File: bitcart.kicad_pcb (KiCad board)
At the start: 4 copper layers, 136.6 x 54.6 mm, 78 parts, among them J1 Conn_01x03, J11 USB_OTG, J17 Molex 470531000, J2 Conn_02x07_Odd_Even, J3 Conn_01x03, Q1 SI7430DP, Q2 MMBTA06LT1G, U1 MP8008, U10 MagJack-A70-112-331N126, U11 EMC2301-1-ACZL-TR, U12 MDT320M01001, U2 FOD817S, U3 750310744, U4 TPD4EUSB30, U5 74LVC1G07SE-7, U6 TL432DBZ, U7 TPD4EUSB30, U8 TPD4EUSB30, U9 74LVC1G07SE-7

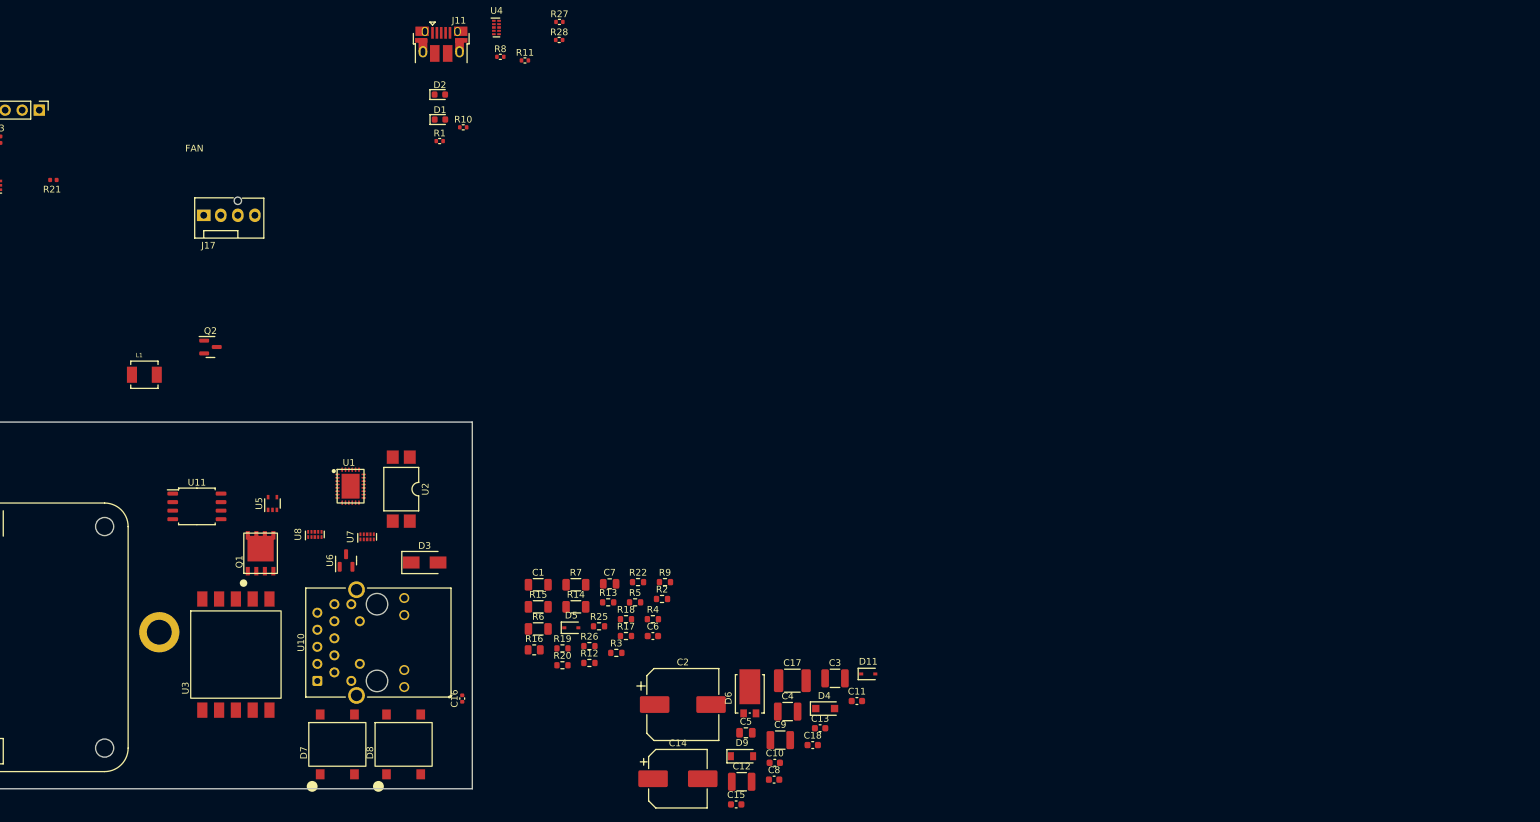
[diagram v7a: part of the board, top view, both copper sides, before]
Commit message: changed PoE transformer to Wurth 7491194912
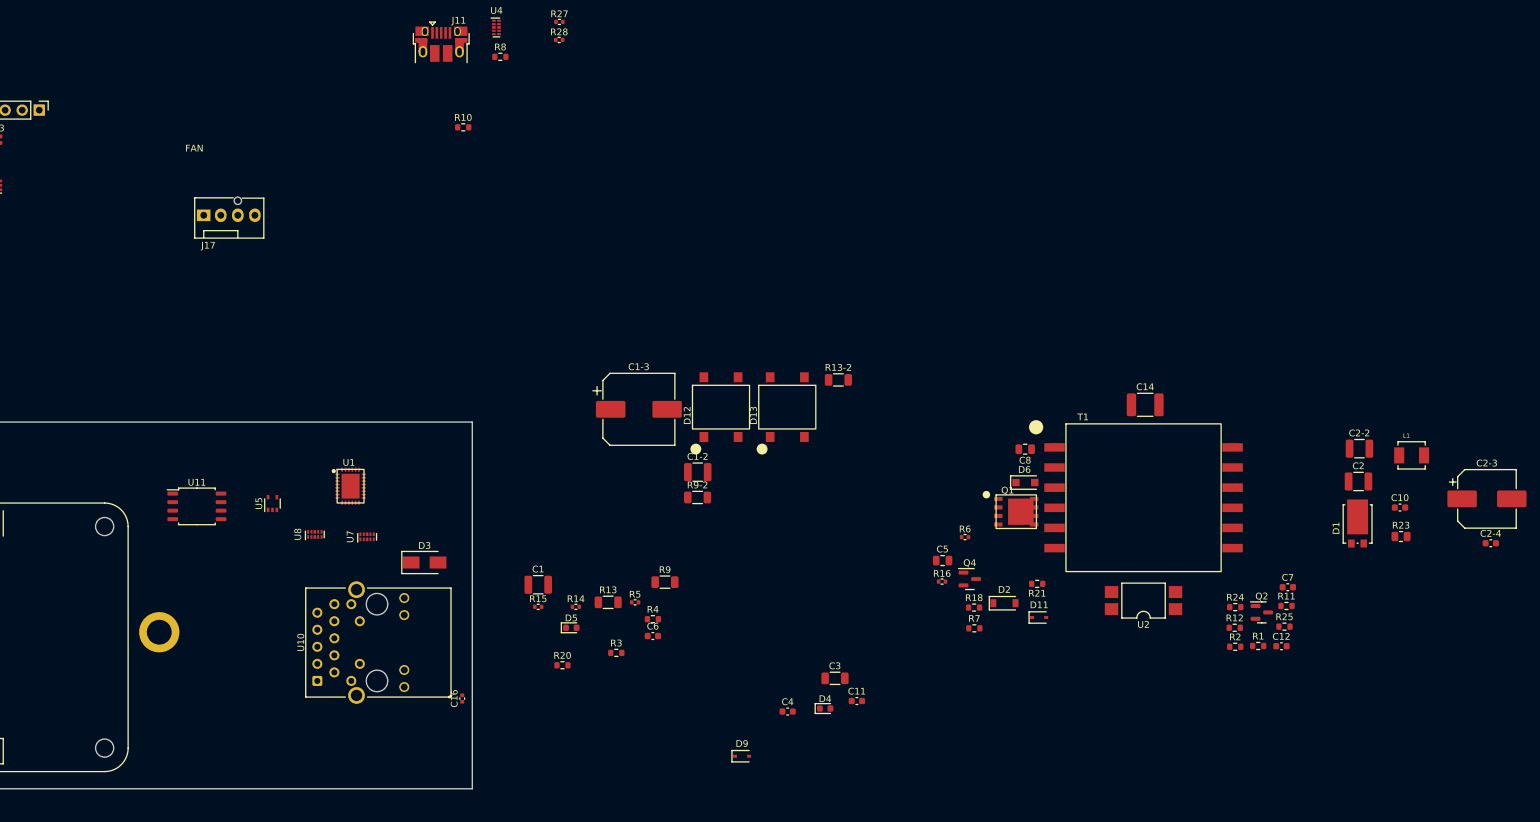
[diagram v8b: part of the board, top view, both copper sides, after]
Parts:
- removed C13: 680pF, Capacitor_SMD:C_0603_1608Metric
- removed C15: 0.1uF, Capacitor_SMD:C_0603_1608Metric
- removed C17: 1nF, 2000V, Capacitor_SMD:C_1812_4532Metric
- removed C18: 1uF, Capacitor_SMD:C_0603_1608Metric
- removed C9: 22uF, Capacitor_SMD:C_1210_3225Metric
- removed D7, D8: DF01S, bitcart:DF01S
- removed R17: 2k, Resistor_SMD:R_0603_1608Metric
- removed R19: 49.9k, Resistor_SMD:R_0603_1608Metric
- removed R22: 1k, Resistor_SMD:R_0603_1608Metric
- removed R26: 191k, Resistor_SMD:R_0603_1608Metric
- removed U3: 750310744, bitcart:750310744
- removed U6: TL432DBZ, Package_TO_SOT_SMD:SOT-23
- added C1-2: 2.2uF, Capacitor_SMD:C_1210_3225Metric, F.Cu at (216.1, 205.1)
- added C1-3: 47uF, Capacitor_SMD:CP_Elec_10x10.5, F.Cu at (207.4, 195.7)
- added C2-2: 22uF, Capacitor_SMD:C_1210_3225Metric, F.Cu at (314.7, 201.6)
- added C2-3: 220uF, Capacitor_SMD:CP_Elec_8x10.5, F.Cu at (333.7, 209.1)
- added C2-4: 0.1uF, Capacitor_SMD:C_0603_1608Metric, F.Cu at (334.2, 215.7)
- added D12: DF01S, bitcart:DF01S, F.Cu at (219.6, 195.4)
- added D13: DF01S, bitcart:DF01S, F.Cu at (229.5, 195.4)
- added Q4: MMBTA06LT1G, Package_TO_SOT_SMD:SOT-23, F.Cu at (256.6, 221.0)
- added R13-2: 20k, Resistor_SMD:R_1206_3216Metric, F.Cu at (237.1, 191.3)
- added R23: 20, Resistor_SMD:R_0805_2012Metric, F.Cu at (320.9, 214.7)
- added R24: 2k, Resistor_SMD:R_0603_1608Metric, F.Cu at (296.2, 225.2)
- added R9-2: 0.082, Resistor_SMD:R_1206_3216Metric, F.Cu at (216.1, 208.9)
- added T1: 7491194912, bitcart:7491194912, F.Cu at (282.5, 208.9)
- C1: value 0.1uF, 100V -> 2.2uF; footprint Resistor_SMD:R_1206_3216Metric -> Capacitor_SMD:C_1210_3225Metric
- C10: value 0.1uF -> 0.47nF
- C12: value 22uF -> 680pF; footprint Capacitor_SMD:C_1210_3225Metric -> Capacitor_SMD:C_0603_1608Metric
- C14: value 220uF -> 1nF, 2000V; footprint Capacitor_SMD:CP_Elec_8x10.5 -> Capacitor_SMD:C_1812_4532Metric
- C2: value 47uF -> 22uF; footprint Capacitor_SMD:CP_Elec_10x10.5 -> Capacitor_SMD:C_1210_3225Metric
- C3: value 2.2uF -> 0.1uF, 100V; footprint Capacitor_SMD:C_1210_3225Metric -> Resistor_SMD:R_1206_3216Metric
- C4: value 2.2uF -> 1uF; footprint Capacitor_SMD:C_1210_3225Metric -> Capacitor_SMD:C_0603_1608Metric
- C5: value 0.1uF -> 4.7uF
- C7: value 4.7uF -> 0.1uF; footprint Capacitor_SMD:C_0805_2012Metric -> Capacitor_SMD:C_0603_1608Metric
- C8: value 0.47nF -> 0.1uF; footprint Capacitor_SMD:C_0603_1608Metric -> Capacitor_SMD:C_0805_2012Metric
- D1: value LED Red -> SBR8U60P5-13; footprint LED_SMD:LED_0603_1608Metric -> bitcart:SBR8U60P5-13
- D2: value LED Green -> 9.1V; footprint LED_SMD:LED_0603_1608Metric -> Diode_SMD:D_SOD-123
- D4: value BAV21 -> LED Green; footprint Diode_SMD:D_SOD-123F -> LED_SMD:LED_0603_1608Metric
- D5: value 1N4148WS -> LED Red; footprint Diode_SMD:D_SOD-323 -> LED_SMD:LED_0603_1608Metric
- D6: value SBR8U60P5-13 -> BAV21; footprint bitcart:SBR8U60P5-13 -> Diode_SMD:D_SOD-123F
- D9: value 9.1V -> 1N4148WS; footprint Diode_SMD:D_SOD-123 -> Diode_SMD:D_SOD-323
- Q2: value MMBTA06LT1G -> TL432DBZ
- R1: value 1k -> 191k; footprint Resistor_SMD:R_0402_1005Metric -> Resistor_SMD:R_0603_1608Metric
- R10: value 1k -> 4.99; footprint Resistor_SMD:R_0402_1005Metric -> Resistor_SMD:R_0603_1608Metric
- R11: value 2.2K 1% -> 49.9k; footprint Resistor_SMD:R_0402_1005Metric -> Resistor_SMD:R_0603_1608Metric
- R12: value 4.99 -> 6.8k
- R13: value 10k -> 20k; footprint Resistor_SMD:R_0603_1608Metric -> Resistor_SMD:R_1206_3216Metric
- R14, R15: value 0.082 -> 2.2K 1%; footprint Resistor_SMD:R_1206_3216Metric -> Resistor_SMD:R_0402_1005Metric
- R16: value 20 -> 36K 1%; footprint Resistor_SMD:R_0805_2012Metric -> Resistor_SMD:R_0402_1005Metric
- R18: value 6.8k -> 1k
- R2: value 28.7 -> 191k
- R20: value 10 -> 4.99
- R21: value 36K 1% -> 10k; footprint Resistor_SMD:R_0402_1005Metric -> Resistor_SMD:R_0603_1608Metric
- R25: value 191k -> 10
- R4: value 9.31k -> 28.7
- R5: value 100k -> 1k; footprint Resistor_SMD:R_0603_1608Metric -> Resistor_SMD:R_0402_1005Metric
- R6: value 20k -> 1k; footprint Resistor_SMD:R_1206_3216Metric -> Resistor_SMD:R_0402_1005Metric
- R7: value 20k -> 100k; footprint Resistor_SMD:R_1206_3216Metric -> Resistor_SMD:R_0603_1608Metric
- R8: value 2.2K 1% -> 9.31k; footprint Resistor_SMD:R_0402_1005Metric -> Resistor_SMD:R_0603_1608Metric
- R9: value 4.99 -> 0.082; footprint Resistor_SMD:R_0603_1608Metric -> Resistor_SMD:R_1206_3216Metric
- moved L1 189.1 mm to (322.4, 202.6)
- moved Q2 161.5 mm to (300.1, 226.0)
- moved R21 158.4 mm to (266.7, 221.7)
- moved D1 149.4 mm to (314.4, 212.8)
- moved R1 143.2 mm to (299.6, 231.0)
- moved R11 139.5 mm to (303.8, 225.0)
- moved D2 113.2 mm to (261.8, 224.6)
- moved Q1 112.7 mm to (263.6, 211.0), turned to 0 degrees
- moved U2 111.8 mm to (282.5, 224.2), turned to 180 degrees
- moved C2 106.0 mm to (314.5, 206.5)
- moved R25 102.1 mm to (303.5, 228.1)
- moved C7 101.0 mm to (304.0, 222.2)
- moved C10 100.6 mm to (320.7, 210.4)
- moved R12 96.3 mm to (296.1, 228.3)
- moved C14 89.1 mm to (282.8, 195.1)
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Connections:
- C1 pad 2: /PoE/VSS -> /PoE/GND1
- C10 pad 1: /PoE/W4 -> Net-(C10-Pad1)
- C12 pad 1: Net-(C9-Pad1) -> Net-(C12-Pad1)
- C12 pad 2: GND -> Net-(C11-Pad2)
- C14 pad 1: /+5v -> /PoE/GND1
- C2 pad 1: /PoE/VDD -> Net-(C2-Pad1)
- C2 pad 2: /PoE/GND1 -> GND
- C3 pad 2: /PoE/GND1 -> /PoE/VSS
- C4 pad 1: /PoE/VDD -> /PoE/VIN
- C5 pad 1: /PoE/VDD -> Net-(C5-Pad1)
- C5 pad 2: Net-(C5-Pad2) -> /PoE/GND1
- C7 pad 1: Net-(C7-Pad1) -> /PoE/W4
- C7 pad 2: /PoE/GND1 -> Net-(R11-Pad2)
- C8 pad 1: Net-(C8-Pad1) -> /PoE/VDD
- D1 pad 1: Net-(D1-Pad1) -> Net-(C2-Pad1)
- D1 pad 2: /+3.3v -> Net-(C10-Pad1)
- D2 pad 2: /+3.3v -> /PoE/GND1
- D4 pad 1: Net-(C5-Pad2) -> Net-(D4-Pad1)
- D4 pad 2: /PoE/W1 -> /+3.3v
- D5 pad 2: Net-(D5-Pad2) -> /+3.3v
- D6 pad 1: Net-(C9-Pad1) -> Net-(C8-Pad2)
- D6 pad 2: Net-(C8-Pad1) -> /PoE/W1
- D9 pad 2: /PoE/GND1 -> Net-(D9-Pad2)
- L1 pad 1: Net-(C9-Pad1) -> Net-(C2-Pad1)
- Q1 pad 1: Net-(R12-Pad1) -> Net-(R10-Pad1)
- Q1 pad 2: Net-(R12-Pad1) -> Net-(R10-Pad1)
- Q1 pad 3: Net-(R12-Pad1) -> Net-(R10-Pad1)
- Q1 pad 4: Net-(D5-Pad2) -> Net-(D9-Pad2)
- Q2 pad 1: Net-(D9-Pad1) -> Net-(C11-Pad2)
- Q2 pad 2: /PoE/VIN -> /PoE/W4
- Q2 pad 3: Net-(Q2-Pad3) -> GND
- R1 pad 1: Net-(D2-Pad1) -> Net-(C11-Pad2)
- R1 pad 2: Net-(Module1-Pad21) -> Net-(C12-Pad1)
- R10 pad 1: Net-(D1-Pad1) -> Net-(R10-Pad1)
- R11 pad 1: /CM4_HighSpeed/USBOTG_ID -> Net-(C11-Pad2)
- R11 pad 2: GND -> Net-(R11-Pad2)
- R12 pad 1: Net-(R12-Pad1) -> Net-(C12-Pad1)
- R12 pad 2: Net-(R12-Pad2) -> /PoE/W3
- R13 pad 1: /PoE/GND1 -> Net-(C8-Pad2)
- R13 pad 2: Net-(R13-Pad2) -> /PoE/VDD
- R14 pad 1: /PoE/GND1 -> /CM4_HighSpeed/USBOTG_ID
- R14 pad 2: Net-(R12-Pad1) -> GND
- R15 pad 1: /PoE/GND1 -> Net-(J11-Pad1)
- R15 pad 2: Net-(R12-Pad1) -> /CM4_HighSpeed/USBOTG_ID
- R16 pad 1: Net-(C9-Pad1) -> Net-(J17-Pad3)
- R16 pad 2: Net-(C8-Pad2) -> /+3.3v
- R18 pad 1: Net-(C13-Pad1) -> Net-(Q4-Pad3)
- R18 pad 2: /PoE/W3 -> /PoE/VDD
- R2 pad 1: /PoE/VSS -> GND
- R2 pad 2: Net-(R2-Pad2) -> Net-(C11-Pad2)
- R20 pad 1: Net-(C13-Pad1) -> Net-(D9-Pad2)
- R20 pad 2: /+5v -> Net-(D9-Pad1)
- R21 pad 1: Net-(J17-Pad3) -> /PoE/GND1
- R21 pad 2: /+3.3v -> Net-(R21-Pad2)
- R25 pad 1: Net-(C11-Pad2) -> Net-(C12-Pad1)
- R25 pad 2: Net-(C13-Pad1) -> /+5v
- R4 pad 1: /PoE/GND1 -> /PoE/VSS
- R5 pad 1: Net-(D9-Pad1) -> Net-(D4-Pad1)
- R5 pad 2: /PoE/VDD -> Net-(Module1-Pad21)
- R6 pad 1: Net-(C5-Pad2) -> Net-(D5-Pad1)
- R6 pad 2: /PoE/VDD -> Net-(U5-Pad4)
- R7 pad 1: Net-(C5-Pad2) -> Net-(D2-Pad1)
- R8 pad 1: Net-(J11-Pad1) -> /PoE/GND1
- R8 pad 2: /CM4_HighSpeed/USBOTG_ID -> Net-(R8-Pad2)
- R9 pad 1: Net-(D5-Pad2) -> /PoE/GND1
- R9 pad 2: Net-(D5-Pad1) -> Net-(R10-Pad1)
- U1 pad 10: Net-(R4-Pad2) -> Net-(R8-Pad2)
- U1 pad 12: Net-(R13-Pad2) -> Net-(R21-Pad2)
- U1 pad 19: Net-(R12-Pad2) -> Net-(R10-Pad2)
- U1 pad 26: Net-(R2-Pad2) -> Net-(R4-Pad2)
- U1 pad 6: Net-(D5-Pad1) -> Net-(D9-Pad1)
- U1 pad 7: Net-(C7-Pad1) -> Net-(C5-Pad1)
- U5 pad 4: Net-(R10-Pad2) -> Net-(U5-Pad4)
